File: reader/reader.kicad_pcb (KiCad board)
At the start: 2 copper layers, 77.5 x 80 mm, 58 parts, among them J1 USB_B_Mini, J2 swd, J3 Conn_01x05, J4 v_sup, Q1 CPH3350-TL-W, SW1 SW_Push, U1 BA33BC0FP-E2, U2 ST25R95, U3 STM32G051GxU, U4 FC2004C03-NSWBBW-91*E, Y1 27.12MHz

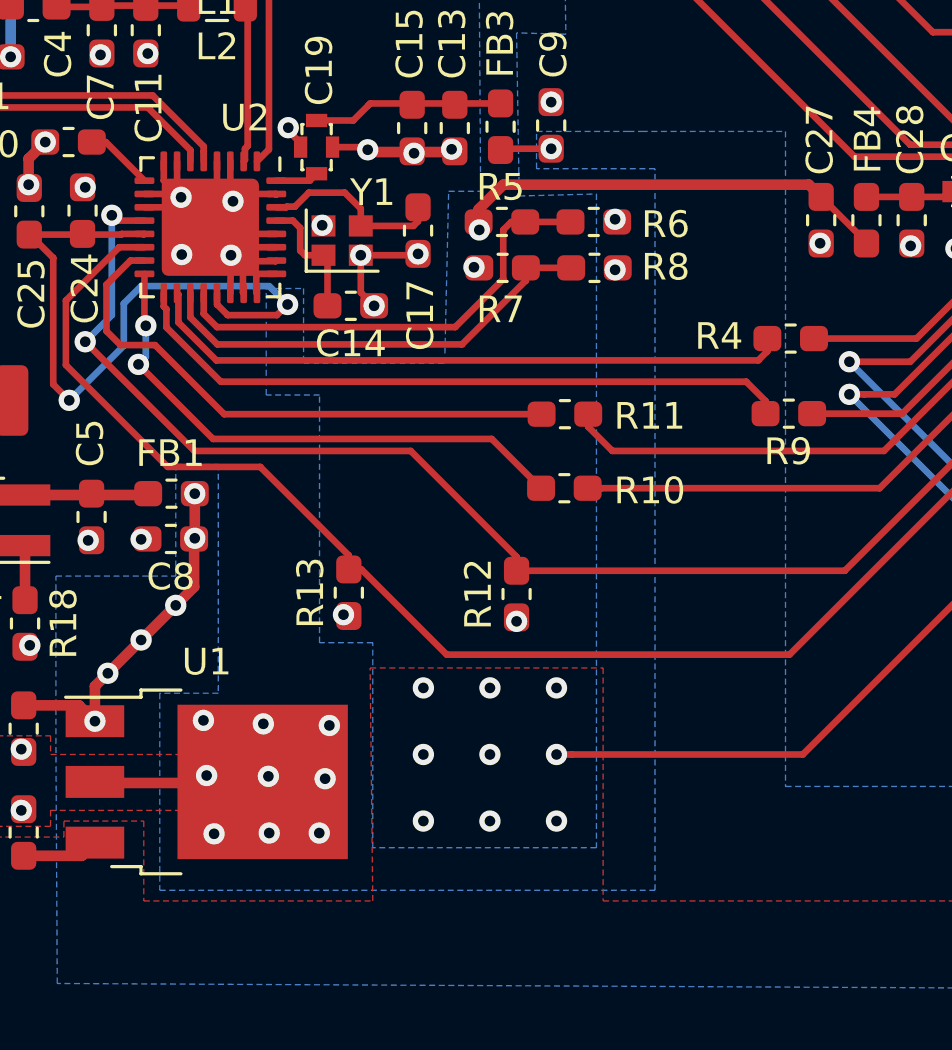
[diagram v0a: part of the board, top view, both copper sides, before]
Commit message: Use solder bride instead of 0ohm
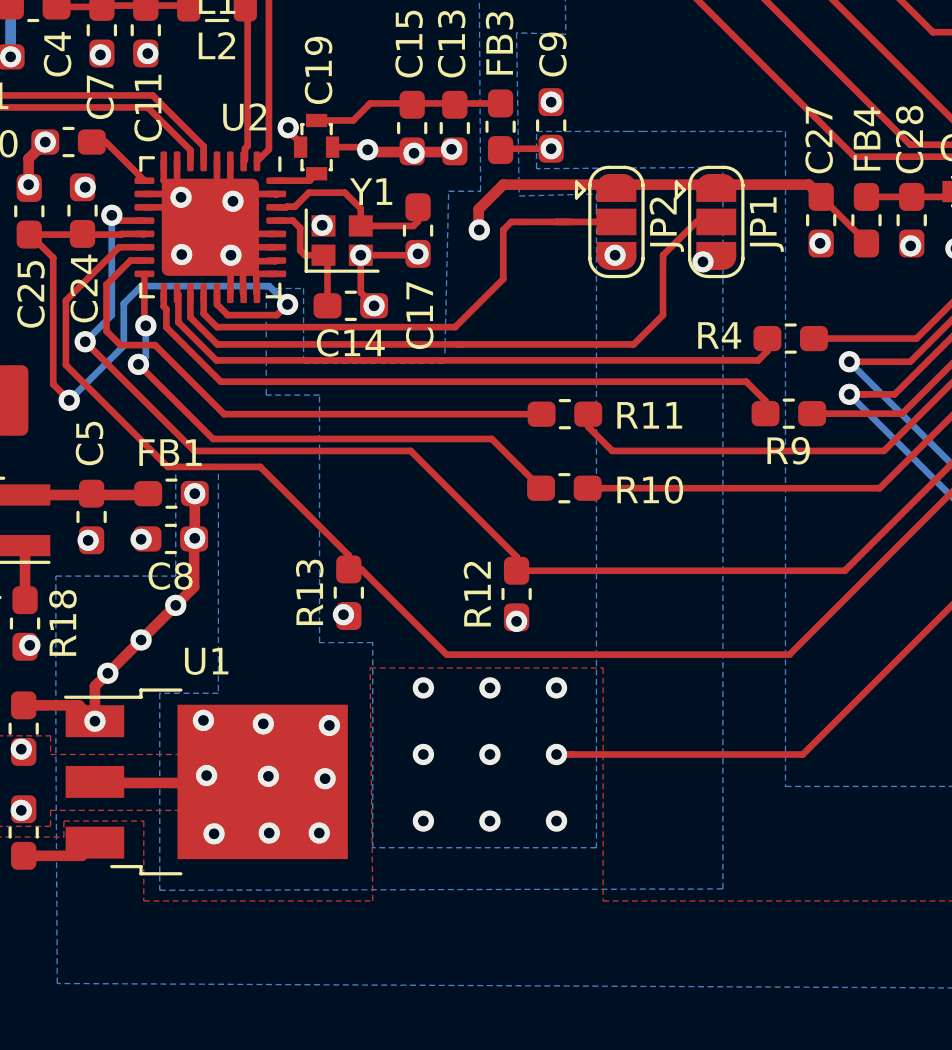
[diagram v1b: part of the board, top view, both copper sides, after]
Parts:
- removed R5, R6, R7, R8: 0, Resistor_SMD:R_0603_1608Metric_Pad1.05x0.95mm_HandSolder
- added JP1: xx, Jumper:SolderJumper-3_P1.3mm_Open_RoundedPad1.0x1.5mm, F.Cu at (148.5, 107.5)
- added JP2: xx, Jumper:SolderJumper-3_P1.3mm_Open_RoundedPad1.0x1.5mm, F.Cu at (144.8, 107.5)
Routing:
- net /rfid_ss0: track 17.1 -> 24.4 mm
- net /rfid_ss1: track 17.5 -> 19.7 mm
- net +3V3: vias 15 -> 14
